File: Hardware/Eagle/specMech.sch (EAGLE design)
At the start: 78 parts, among them J1 PINHD-1X8-MOLEX-SHROUD, J2 JST-2-PIN-2B-PH-K-S(LF)(SN), J3 PINHD-1X8-MOLEX-SHROUD, J4 PINHD-1X8-MOLEX-SHROUD, J6 Molex 0022232081, J8 Molex 0022232081, U1 MCP23008-E/SO, U10 ADS1115, U11 MCP23008-E/SO, U12 74HC2G17TSSOP-6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

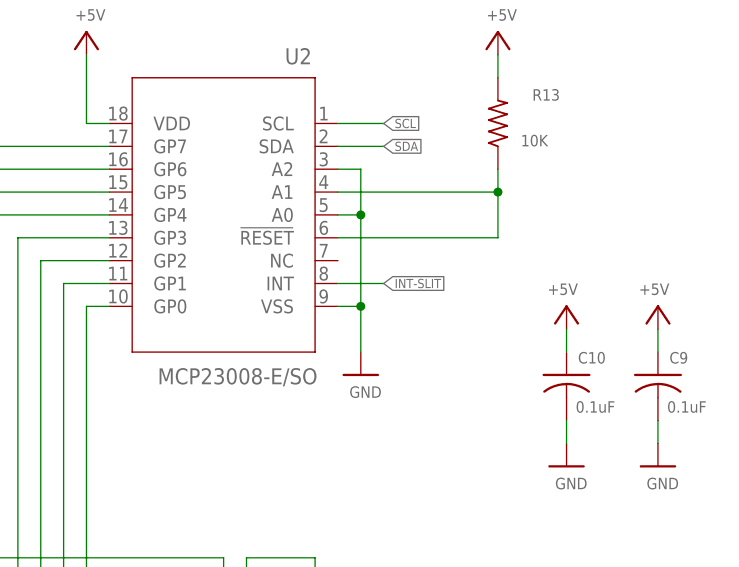
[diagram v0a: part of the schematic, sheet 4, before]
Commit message: Changed FRAM footprint to allow both IC sizes
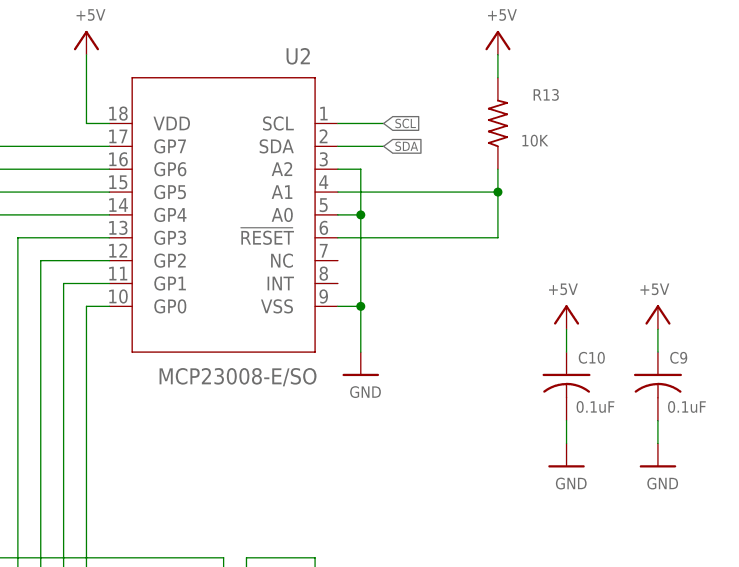
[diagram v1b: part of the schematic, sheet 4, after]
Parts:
- U14: device AUmlib:MB85RC512 -> AUmlib:MB85RC512FPT-FP-DUALWIDTH
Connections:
- removed net INT-SLIT: U2.INT
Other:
- note added: "Do not connect a pullup to /RST (50k ohm inside) RST is an output"
- note added: "Pin 1 location 3.58, 4.48 in PINS #1-13 read the slithead magnets PIN 15 used to go to the fan control These are not used now? PIN# (not true; just examples) 17 - Shutter Open 19 - Shutter Close 21 - Left Hartmann Open 23 - Left Hartmann Close 25 - Right Hartmann Open 27 - Right Hartmann Close 29 - Air Pressure On 31 - Not used (was reset)"
- note removed: "Do not connect a pullup to /RST (50k ohm inside)"
- note removed: "Pin 1 location 3.58, 4.48 in PINS #1-13 read the slithead magnets PIN 15 used to go to the fan control These are not used now? PIN# (not true; just examples) 17 - Shutter Open 19 - Shutter Close 21 - Left Hartmann Open 23 - Left Hartmann Close 25 - Right Hartmann Open 27 - Right Hartmann Close 29 - Not used 31 - Not used"

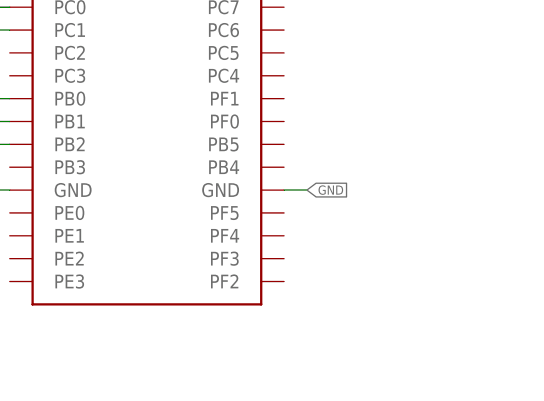
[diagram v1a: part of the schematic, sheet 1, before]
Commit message: Added spectrograph selection jumper
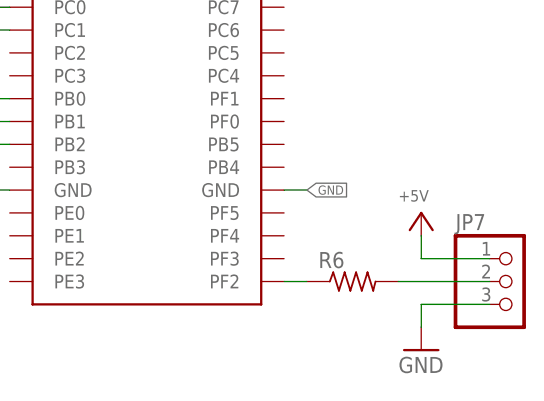
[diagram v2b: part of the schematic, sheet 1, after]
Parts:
- added JP7: (no value), AUmlib:PINHD-1X3
- added R6: (no value), AUmlib:R-US_R0805
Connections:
- new net N$6: CNANO1.PF2, R6.1
- new net N$7: JP7.2, R6.2
- net +5V: now also JP7.1
- net GND: now also JP7.3
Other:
- note added: "Spectrograph Number Select"

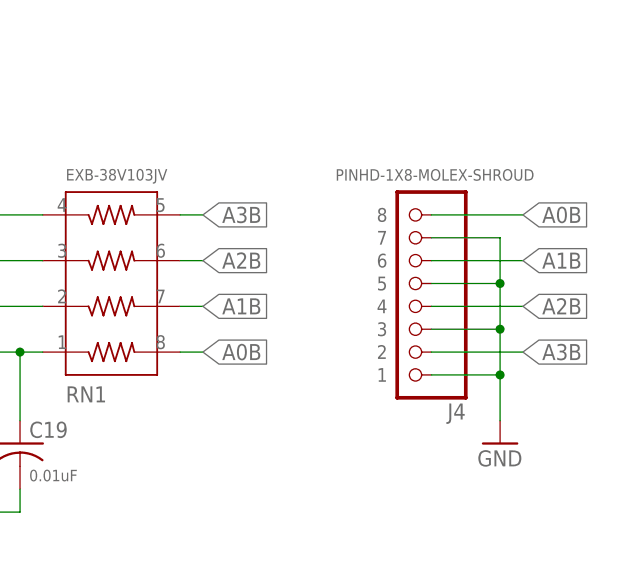
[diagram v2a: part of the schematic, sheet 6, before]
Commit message: Fixed label errors in humidity sensor input lines
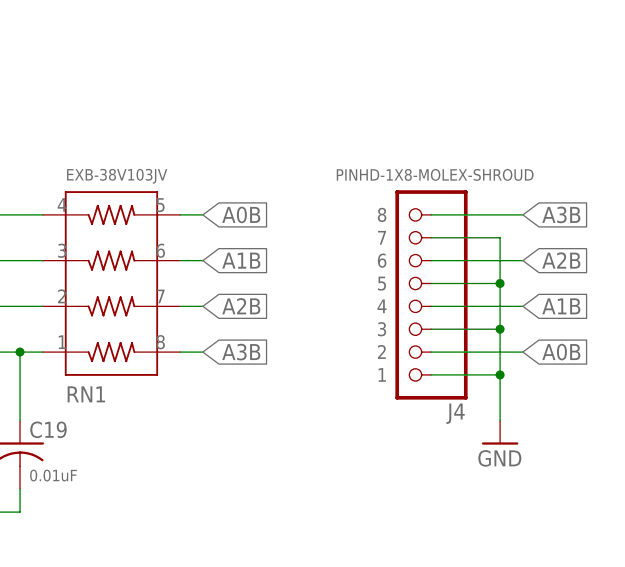
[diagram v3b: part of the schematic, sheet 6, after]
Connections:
- net A0B: now also J4.2, RN1.5; no longer J4.8, RN1.8
- net A1B: now also J4.4, RN1.6; no longer J4.6, RN1.7
- net A2B: now also J4.6, RN1.7; no longer J4.4, RN1.6
- net A3B: now also J4.8, RN1.8; no longer J4.2, RN1.5
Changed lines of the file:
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@@
-</segment>
-</net>
-<net name="A0B" class="0">
-<segment>
-<pinref part="RN1" gate="G$1" pin="8"/>
-<wire x1="208.28" y1="96.52" x2="210.82" y2="96.52" width="0.1524" layer="91"/>
-<label x="210.82" y="96.52" size="1.778" layer="95" rot="MR180" xref="yes"/>
-</segment>
-<segment>
-<pinref part="J4" gate="G$1" pin="8"/>
-<wire x1="236.22" y1="111.76" x2="246.38" y2="111.76" width="0.1524" layer="91"/>
-<label x="246.38" y="111.76" size="1.778" layer="95" rot="MR180" xref="yes"/>
-</segment>
-</net>
-<net name="A1B" class="0">
-<segment>
-<pinref part="RN1" gate="G$1" pin="7"/>
-<wire x1="208.28" y1="101.6" x2="210.82" y2="101.6" width="0.1524" layer="91"/>
-<label x="210.82" y="101.6" size="1.778" layer="95" rot="MR180" xref="yes"/>
-</segment>
-<segment>
-<pinref part="J4" gate="G$1" pin="6"/>
-<wire x1="236.22" y1="106.68" x2="246.38" y2="106.68" width="0.1524" layer="91"/>
-<label x="246.38" y="106.68" size="1.778" layer="95" rot="MR180" xref="yes"/>
-</segment>
-</net>
-<net name="A2B" class="0">
-<segment>
-<pinref part="RN1" gate="G$1" pin="6"/>
-<wire x1="208.28" y1="106.68" x2="210.82" y2="106.68" width="0.1524" layer="91"/>
-<label x="210.82" y="106.68" size="1.778" layer="95" rot="MR180" xref="yes"/>
-</segment>
-<segment>
-<pinref part="J4" gate="G$1" pin="4"/>
-<wire x1="236.22" y1="101.6" x2="246.38" y2="101.6" width="0.1524" layer="91"/>
-<label x="246.38" y="101.6" size="1.778" layer="95" rot="MR180" xref="yes"/>
-</segment>
-</net>
-<net name="A3B" class="0">
-<segment>
-<pinref part="RN1" gate="G$1" pin="5"/>
-<wire x1="208.28" y1="111.76" x2="210.82" y2="111.76" width="0.1524" layer="91"/>
-<label x="210.82" y="111.76" size="1.778" layer="95" rot="MR180" xref="yes"/>
-</segment>
-<segment>
-<pinref part="J4" gate="G$1" pin="2"/>
-<wire x1="236.22" y1="96.52" x2="246.38" y2="96.52" width="0.1524" layer="91"/>
-<label x="246.38" y="96.52" size="1.778" layer="95" rot="MR180" xref="yes"/>
 </segment>
 </net>
@@
 </segment>
 </net>
+<net name="A0B" class="0">
+<segment>
+<pinref part="RN1" gate="G$1" pin="5"/>
+<wire x1="208.28" y1="111.76" x2="210.82" y2="111.76" width="0.1524" layer="91"/>
+<label x="210.82" y="111.76" size="1.778" layer="95" xref="yes"/>
+</segment>
+<segment>
+<pinref part="J4" gate="G$1" pin="2"/>
+<wire x1="236.22" y1="96.52" x2="246.38" y2="96.52" width="0.1524" layer="91"/>
+<label x="246.38" y="96.52" size="1.778" layer="95" xref="yes"/>
+</segment>
+</net>
+<net name="A1B" class="0">
+<segment>
+<pinref part="RN1" gate="G$1" pin="6"/>
+<wire x1="208.28" y1="106.68" x2="210.82" y2="106.68" width="0.1524" layer="91"/>
+<label x="210.82" y="106.68" size="1.778" layer="95" xref="yes"/>
+</segment>
+<segment>
+<pinref part="J4" gate="G$1" pin="4"/>
+<wire x1="236.22" y1="101.6" x2="246.38" y2="101.6" width="0.1524" layer="91"/>
+<label x="246.38" y="101.6" size="1.778" layer="95" xref="yes"/>
+</segment>
+</net>
+<net name="A2B" class="0">
+<segment>
+<pinref part="RN1" gate="G$1" pin="7"/>
+<wire x1="208.28" y1="101.6" x2="210.82" y2="101.6" width="0.1524" layer="91"/>
+<label x="210.82" y="101.6" size="1.778" layer="95" xref="yes"/>
+</segment>
+<segment>
+<pinref part="J4" gate="G$1" pin="6"/>
+<wire x1="236.22" y1="106.68" x2="246.38" y2="106.68" width="0.1524" layer="91"/>
+<label x="246.38" y="106.68" size="1.778" layer="95" xref="yes"/>
+</segment>
+</net>
+<net name="A3B" class="0">
+<segment>
+<pinref part="RN1" gate="G$1" pin="8"/>
+<wire x1="208.28" y1="96.52" x2="210.82" y2="96.52" width="0.1524" layer="91"/>
+<label x="210.82" y="96.52" size="1.778" layer="95" xref="yes"/>
+</segment>
+<segment>
+<pinref part="J4" gate="G$1" pin="8"/>
+<wire x1="236.22" y1="111.76" x2="246.38" y2="111.76" width="0.1524" layer="91"/>
+<label x="246.38" y="111.76" size="1.778" layer="95" xref="yes"/>
+</segment>
+</net>

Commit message: Added test points, changed conflicting i2c address
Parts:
- added TP1, TP5: TP5000-TESTPOINT-BLK, AUmlib:TP5000-TESTPOINT-BLK
- added TP2: TP5000-TESTPOINT-RED, AUmlib:TP5000-TESTPOINT-RED
- added TP3: TP5000-TESTPOINT-BLU, AUmlib:TP5000-TESTPOINT-BLU
- added TP4: TP5000-TESTPOINT-YEL, AUmlib:TP5000-TESTPOINT-YEL
- added TP6: TP5000-TESTPOINT-ORG, AUmlib:TP5000-TESTPOINT-ORG
- J7: value (none) -> Lantronix XPORT
- R10, R6: value (none) -> 10K
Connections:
- net +12V: now also TP6.1
- net +5V: now also TP2.1
- net GND: now also TP1.1, TP5.1; no longer U11.A0, U11.A1, U11.A2
- net N$5: now also U11.A0, U11.A1, U11.A2
- net OL/RST: now also CNANO1.PD6
- net SCL: now also TP4.1
- net SDA: now also TP3.1

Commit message: Added some part values, changed date on label
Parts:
- JP1: value (none) -> 2x5 pinhdr
- JP2: value (none) -> 1x6 pinhdr
- JP3: value (none) -> 2x18 pinhdr
- JP4: value (none) -> 1x2 pinhdr
- JP5, JP7: value (none) -> 1x3 pinhdr
- JP6: value (none) -> 2x3 pinhdr
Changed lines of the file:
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@@
 <setting verticaltext="up"/>
 </settings>
-<grid distance="0.1" unitdist="inch" unit="inch" style="lines" multiple="1" display="yes" altdistance="0.01" altunitdist="inch" altunit="inch"/>
+<grid distance="0.1" unitdist="inch" unit="inch" style="lines" multiple="1" display="no" altdistance="0.01" altunitdist="inch" altunit="inch"/>
 <layers>
 <layer number="1" name="Top" color="4" fill="1" visible="no" active="no"/>
@@
 <part name="GND10" library="AUmlib" library_urn="urn:adsk.eagle:library:9166017" deviceset="GND" device=""/>
 <part name="SUPPLY1" library="AUmlib" library_urn="urn:adsk.eagle:library:9166017" deviceset="+12V" device=""/>
-<part name="JP3" library="AUmlib" library_urn="urn:adsk.eagle:library:9166017" deviceset="PINHD-2X16" device="" package3d_urn="urn:adsk.eagle:package:22431/2"/>
-<part name="JP4" library="AUmlib" library_urn="urn:adsk.eagle:library:9166017" deviceset="PINHD-1X2" device="" package3d_urn="urn:adsk.eagle:package:15461696/1"/>
+<part name="JP3" library="AUmlib" library_urn="urn:adsk.eagle:library:9166017" deviceset="PINHD-2X16" device="" package3d_urn="urn:adsk.eagle:package:22431/2" value="2x18 pinhdr"/>
+<part name="JP4" library="AUmlib" library_urn="urn:adsk.eagle:library:9166017" deviceset="PINHD-1X2" device="" package3d_urn="urn:adsk.eagle:package:15461696/1" value="1x2 pinhdr"/>
 <part name="GND1" library="AUmlib" library_urn="urn:adsk.eagle:library:9166017" deviceset="GND" device=""/>
 <part name="GND2" library="AUmlib" library_urn="urn:adsk.eagle:library:9166017" deviceset="GND" device=""/>
@@
 <part name="J1" library="AUmlib" library_urn="urn:adsk.eagle:library:9166017" deviceset="PINHD-1X8-MOLEX-SHROUD" device="" package3d_urn="urn:adsk.eagle:package:18132194/5"/>
 <part name="CNANO1" library="AUmlib" library_urn="urn:adsk.eagle:library:9166017" deviceset="CURIOSITYNANO4809" device="" package3d_urn="urn:adsk.eagle:package:15461704/5"/>
-<part name="FRAME1" library="frames" library_urn="urn:adsk.eagle:library:229" deviceset="FRAME_A_L" device=""/>
-<part name="FRAME3" library="frames" library_urn="urn:adsk.eagle:library:229" deviceset="FRAME_A_L" device=""/>
-<part name="FRAME4" library="frames" library_urn="urn:adsk.eagle:library:229" deviceset="FRAME_A_L" device=""/>
-<part name="FRAME5" library="frames" library_urn="urn:adsk.eagle:library:229" deviceset="FRAME_A_L" device=""/>
-<part name="FRAME6" library="frames" library_urn="urn:adsk.eagle:library:229" deviceset="FRAME_A_L" device=""/>
-<part name="FRAME7" library="frames" library_urn="urn:adsk.eagle:library:229" deviceset="FRAME_A_L" device=""/>
-<part name="FRAME8" library="frames" library_urn="urn:adsk.eagle:library:229" deviceset="FRAME_A_L" device=""/>
+<part name="FRAME1" library="frames" library_urn="urn:adsk.eagle:library:229" deviceset="FRAME_A_L" device="" value="Frame_A_L"/>
+<part name="FRAME3" library="frames" library_urn="urn:adsk.eagle:library:229" deviceset="FRAME_A_L" device="" value="Frame_A_L"/>
+<part name="FRAME4" library="frames" library_urn="urn:adsk.eagle:library:229" deviceset="FRAME_A_L" device="" value="Frame_A_L"/>
+<part name="FRAME5" library="frames" library_urn="urn:adsk.eagle:library:229" deviceset="FRAME_A_L" device="" value="Frame_A_L"/>
+<part name="FRAME6" library="frames" library_urn="urn:adsk.eagle:library:229" deviceset="FRAME_A_L" device="" value="Frame_A_L"/>
+<part name="FRAME7" library="frames" library_urn="urn:adsk.eagle:library:229" deviceset="FRAME_A_L" device="" value="Frame_A_L"/>
+<part name="FRAME8" library="frames" library_urn="urn:adsk.eagle:library:229" deviceset="FRAME_A_L" device="" value="Frame_A_L"/>
 <part name="J3" library="AUmlib" library_urn="urn:adsk.eagle:library:9166017" deviceset="PINHD-1X8-MOLEX-SHROUD" device="" package3d_urn="urn:adsk.eagle:package:18132194/5"/>
 <part name="GND27" library="AUmlib" library_urn="urn:adsk.eagle:library:9166017" deviceset="GND" device=""/>
@@
 <part name="GND37" library="AUmlib" library_urn="urn:adsk.eagle:library:9166017" deviceset="GND" device=""/>
 <part name="PS1" library="AUmlib" library_urn="urn:adsk.eagle:library:9166017" deviceset="OKI-78SR-5/1.5-W36-C" device="" package3d_urn="urn:adsk.eagle:package:24308288/2"/>
-<part name="FRAME11" library="frames" library_urn="urn:adsk.eagle:library:229" deviceset="FRAME_A_L" device=""/>
-<part name="JP6" library="AUmlib" library_urn="urn:adsk.eagle:library:9166017" deviceset="PINHD-2X3" device="" package3d_urn="urn:adsk.eagle:package:24493429/1"/>
-<part name="JP1" library="AUmlib" library_urn="urn:adsk.eagle:library:9166017" deviceset="PINHD-2X5" device="" package3d_urn="urn:adsk.eagle:package:24435877/1"/>
+<part name="FRAME11" library="frames" library_urn="urn:adsk.eagle:library:229" deviceset="FRAME_A_L" device="" value="Frame_A_L"/>
+<part name="JP6" library="AUmlib" library_urn="urn:adsk.eagle:library:9166017" deviceset="PINHD-2X3" device="" package3d_urn="urn:adsk.eagle:package:24493429/1" value="2x3 pinhdr"/>
+<part name="JP1" library="AUmlib" library_urn="urn:adsk.eagle:library:9166017" deviceset="PINHD-2X5" device="" package3d_urn="urn:adsk.eagle:package:24435877/1" value="2x5 pinhdr"/>
 <part name="U12" library="AUmlib" library_urn="urn:adsk.eagle:library:9166017" deviceset="74HC2G17" device="TSSOP-6" package3d_urn="urn:adsk.eagle:package:9152015/2"/>
 <part name="GND28" library="AUmlib" library_urn="urn:adsk.eagle:library:9166017" deviceset="GND" device=""/>
@@
 <part name="SUPPLY10" library="AUmlib" library_urn="urn:adsk.eagle:library:9166017" deviceset="+12V" device=""/>
 <part name="U13" library="AUmlib" library_urn="urn:adsk.eagle:library:9166017" deviceset="ISO7421DR" device="TI-SOIC-D8" package3d_urn="urn:adsk.eagle:package:16444440/1" value="ISO7421DR"/>
-<part name="JP2" library="AUmlib" library_urn="urn:adsk.eagle:library:9166017" deviceset="PINHD-1X6" device="" package3d_urn="urn:adsk.eagle:package:24493396/1"/>
+<part name="JP2" library="AUmlib" library_urn="urn:adsk.eagle:library:9166017" deviceset="PINHD-1X6" device="" package3d_urn="urn:adsk.eagle:package:24493396/1" value="1x6 pinhdr"/>
 <part name="C24" library="AUmlib" library_urn="urn:adsk.eagle:library:9166017" deviceset="C-US" device="C0805" package3d_urn="urn:adsk.eagle:package:4021265/3" value="0.1uF"/>
 <part name="C25" library="AUmlib" library_urn="urn:adsk.eagle:library:9166017" deviceset="C-US" device="C0805" package3d_urn="urn:adsk.eagle:package:4021265/3" value="0.1uF"/>
@@
 <part name="GND41" library="AUmlib" library_urn="urn:adsk.eagle:library:9166017" deviceset="GND" device=""/>
 <part name="GND42" library="AUmlib" library_urn="urn:adsk.eagle:library:9166017" deviceset="GND" device=""/>
-<part name="JP5" library="AUmlib" library_urn="urn:adsk.eagle:library:9166017" deviceset="PINHD-1X3" device="" package3d_urn="urn:adsk.eagle:package:21589412/1"/>
+<part name="JP5" library="AUmlib" library_urn="urn:adsk.eagle:library:9166017" deviceset="PINHD-1X3" device="" package3d_urn="urn:adsk.eagle:package:21589412/1" value="1x3 pinhdr"/>
 <part name="U7" library="AUmlib" library_urn="urn:adsk.eagle:library:9166017" deviceset="LTC4311ISC6TRPBF" device="" package3d_urn="urn:adsk.eagle:package:24435366/2"/>
 <part name="C22" library="AUmlib" library_urn="urn:adsk.eagle:library:9166017" deviceset="C-US" device="C0805" package3d_urn="urn:adsk.eagle:package:4021265/3" value="0.1uF"/>
@@
 <part name="GND4" library="AUmlib" library_urn="urn:adsk.eagle:library:9166017" deviceset="GND" device=""/>
 <part name="P+27" library="AUmlib" library_urn="urn:adsk.eagle:library:9166017" deviceset="+5V" device=""/>
-<part name="JP7" library="AUmlib" library_urn="urn:adsk.eagle:library:9166017" deviceset="PINHD-1X3" device="" package3d_urn="urn:adsk.eagle:package:21589412/1"/>
+<part name="JP7" library="AUmlib" library_urn="urn:adsk.eagle:library:9166017" deviceset="PINHD-1X3" device="" package3d_urn="urn:adsk.eagle:package:21589412/1" value="1x3 pinhdr"/>
 <part name="R6" library="AUmlib" library_urn="urn:adsk.eagle:library:9166017" deviceset="R-US_" device="R0805" package3d_urn="urn:adsk.eagle:package:4021199/4" value="10K"/>
 <part name="P+28" library="AUmlib" library_urn="urn:adsk.eagle:library:9166017" deviceset="+5V" device=""/>
 <part name="GND43" library="AUmlib" library_urn="urn:adsk.eagle:library:9166017" deviceset="GND" device=""/>
-<part name="FRAME2" library="frames" library_urn="urn:adsk.eagle:library:229" deviceset="FRAME_A_L" device=""/>
+<part name="FRAME2" library="frames" library_urn="urn:adsk.eagle:library:229" deviceset="FRAME_A_L" device="" value="Frame_A_L"/>
 <part name="TP1" library="AUmlib" library_urn="urn:adsk.eagle:library:9166017" deviceset="TP5000-TESTPOINT-BLK" device="" package3d_urn="urn:adsk.eagle:package:24642442/4"/>
 <part name="TP2" library="AUmlib" library_urn="urn:adsk.eagle:library:9166017" deviceset="TP5000-TESTPOINT-RED" device="" package3d_urn="urn:adsk.eagle:package:24643663/2"/>
@@
 <instance part="JP1" gate="A" x="40.64" y="132.08" smashed="yes" rot="R90">
 <attribute name="NAME" x="36.83" y="144.145" size="1.778" layer="95" rot="R180"/>
-<attribute name="VALUE" x="50.8" y="125.73" size="1.778" layer="96" rot="R90"/>
+<attribute name="VALUE" x="50.8" y="128.27" size="1.778" layer="96" rot="R90"/>
 </instance>
 <instance part="U12" gate="A" x="40.64" y="104.14" smashed="yes">

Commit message: Submitted this one (Rev0) for fab to Oshpark
2020-11-12 specMech Rev0
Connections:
- net FILT5V renamed ADCVDD
- net N$27 renamed GND1
- net VBAT1 renamed VBAT
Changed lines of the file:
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@@
 </segment>
 </net>
-<net name="VBAT1" class="0">
+<net name="VBAT" class="0">
 <segment>
 <pinref part="U6" gate="A" pin="VBAT"/>
@@
 </segment>
 </net>
-<net name="FILT5V" class="0">
+<net name="ADCVDD" class="0">
 <segment>
 <pinref part="C12" gate="G$1" pin="1"/>
@@
 </segment>
 </net>
-<net name="FILT5V" class="0">
+<net name="ADCVDD" class="0">
 <segment>
 <pinref part="U11" gate="A" pin="VDD"/>
@@
 <wire x1="266.7" y1="157.48" x2="83.82" y2="157.48" width="0.254" layer="250"/>
 <wire x1="83.82" y1="157.48" x2="83.82" y2="134.62" width="0.254" layer="250"/>
-<text x="246.38" y="129.54" size="2.54" layer="250">Level Shifter</text>
+<text x="243.84" y="129.54" size="2.54" layer="250">Level Shifter</text>
 <text x="144.78" y="137.16" size="2.54" layer="250">EtherNET Interface:
 Lantronix XPORT for EtherNET to serial
@@
 </segment>
 </net>
-<net name="N$27" class="0">
+<net name="GND1" class="0">
 <segment>
 <pinref part="JP2" gate="A" pin="4"/>
@@
 <segment>
 <pinref part="U3" gate="A" pin="B2"/>
-<wire x1="218.44" y1="109.22" x2="226.06" y2="109.22" width="0.1524" layer="91"/>
-<label x="226.06" y="109.22" size="1.016" layer="95" xref="yes"/>
-</segment>
-</net>
+<wire x1="218.44" y1="109.22" x2="220.98" y2="109.22" width="0.1524" layer="91"/>
+<label x="220.98" y="109.22" size="1.016" layer="95" xref="yes"/>
+</segment>
+</net>

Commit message: Added future change notes to schematic
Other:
- note added: "Change to 2-pin polarized header"
- note added: "Change to 4-pin Molex 22112042 gold pin"
- note added: "Consider isoloator depending on roboclaw 12v handling"
- note added: "Use old RS-232 cabling"
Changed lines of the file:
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@@
 Spikes from chassis ground are shared
 to maintain 3.3 V signaling.</text>
+<text x="190.5" y="167.64" size="1.778" layer="250">Change to 4-pin Molex 22112042 gold pin</text>
+<text x="50.8" y="48.26" size="1.778" layer="250">Change to 2-pin
+polarized header</text>
+<text x="53.34" y="144.78" size="1.778" layer="250">Use old RS-232
+cabling</text>
+<text x="25.4" y="88.9" size="1.778" layer="250">Consider isoloator depending
+on roboclaw 12v handling</text>
 </plain>
 <instances>

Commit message: Printed 2020-11-12 Schematic
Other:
- note added: "Add 10uF input filter"
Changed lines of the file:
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@@
 <drawing>
 <settings>
-<setting alwaysvectorfont="no"/>
+<setting alwaysvectorfont="yes"/>
 <setting verticaltext="up"/>
 </settings>
@@
 <wire x1="154.94" y1="101.6" x2="154.94" y2="160.02" width="0.254" layer="250"/>
 <text x="175.26" y="154.94" size="2.54" layer="250">Power for USB isolator</text>
+<text x="63.5" y="137.16" size="1.778" layer="250">Add 10uF input filter</text>
 </plain>
 <instances>
